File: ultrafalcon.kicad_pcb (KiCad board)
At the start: 2 copper layers, 66.3 x 66.3 mm, 1 part, among them SW1 RotaryEncoder

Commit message: jan17 updates
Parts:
- added C1: 0.01uF, ct-kicad:C0402, F.Cu at (147.5, 127.2)
- added C2: 0.01uF, ct-kicad:C0402, F.Cu at (152.5, 127.2)
- added C3: 1uF, ct-kicad:C0402, F.Cu at (158.6, 103.1)
- added H1: MountingHole, MountingHole:MountingHole_3.2mm_M3_Pad_Via, F.Cu at (143.5, 112.0)
- added H2: MountingHole, MountingHole:MountingHole_3.2mm_M3_Pad_Via, F.Cu at (143.5, 87.0)
- added J1: Conn_01x08_Socket, Connector_JST:JST_EH_B8B-EH-A_1x08_P2.50mm_Vertical, F.Cu at (160.0, 100.0)
- added R1: 330, ct-kicad:R0603, F.Cu at (158.2, 127.0)
- added R2: 10k, ct-kicad:R0603, F.Cu at (154.2, 127.0)
- added R3: 10k, ct-kicad:R0603, F.Cu at (145.8, 127.0)
- added R4: 10k, ct-kicad:R0603, F.Cu at (155.9, 127.0)
- added R5: 10k, ct-kicad:R0603, F.Cu at (144.1, 127.0)
- added U1: SK6812MINI-E_C5149201, ct-kicad:YS-SK6812MINI-E-casuanoob, F.Cu at (141.1, 66.9)
- added U10: SK6812MINI-E_C5149201, ct-kicad:YS-SK6812MINI-E-casuanoob, F.Cu at (116.7, 109.2)
- added U11: SK6812MINI-E_C5149201, ct-kicad:YS-SK6812MINI-E-casuanoob, F.Cu at (116.7, 91.3)
- added U12: SK6812MINI-E_C5149201, ct-kicad:YS-SK6812MINI-E-casuanoob, F.Cu at (125.6, 75.9)
- added U13: SK6812MINI-E_C5149201, ct-kicad:YS-SK6812MINI-E-casuanoob, F.Cu at (134.6, 108.5)
- added U14: SK6812MINI-E_C5149201, ct-kicad:YS-SK6812MINI-E-casuanoob, F.Cu at (134.9, 90.9)
- added U15: SK6812MINI-E_C5149201, ct-kicad:YS-SK6812MINI-E-casuanoob, F.Cu at (150.4, 82.4)
- added U16: SK6812MINI-E_C5149201, ct-kicad:YS-SK6812MINI-E-casuanoob, F.Cu at (165.4, 91.5)
- added U17: SK6812MINI-E_C5149201, ct-kicad:YS-SK6812MINI-E-casuanoob, F.Cu at (165.1, 109.1)
- added U18: SK6812MINI-E_C5149201, ct-kicad:YS-SK6812MINI-E-casuanoob, F.Cu at (149.6, 117.6)
- added U2: SK6812MINI-E_C5149201, ct-kicad:YS-SK6812MINI-E-casuanoob, F.Cu at (158.9, 66.9)
- added U3: SK6812MINI-E_C5149201, ct-kicad:YS-SK6812MINI-E-casuanoob, F.Cu at (174.4, 75.9)
- added U4: SK6812MINI-E_C5149201, ct-kicad:YS-SK6812MINI-E-casuanoob, F.Cu at (183.3, 91.3)
- added U5: SK6812MINI-E_C5149201, ct-kicad:YS-SK6812MINI-E-casuanoob, F.Cu at (183.3, 109.2)
- added U6: SK6812MINI-E_C5149201, ct-kicad:YS-SK6812MINI-E-casuanoob, F.Cu at (174.4, 124.7)
- added U7: SK6812MINI-E_C5149201, ct-kicad:YS-SK6812MINI-E-casuanoob, F.Cu at (158.9, 133.6)
- added U8: SK6812MINI-E_C5149201, ct-kicad:YS-SK6812MINI-E-casuanoob, F.Cu at (141.1, 133.6)
- added U9: SK6812MINI-E_C5149201, ct-kicad:YS-SK6812MINI-E-casuanoob, F.Cu at (125.6, 124.7)
- SW1: footprint fingerpunch:PERS56v3 -> ct-kicad:PER60
- moved SW1 2.20 mm to (150.0, 100.0)
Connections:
- SW1 pad A: unconnected-(SW1-PadA) -> Net-(C2-Pad1)
- SW1 pad B: unconnected-(SW1-PadB) -> Net-(C1-Pad1)
- SW1 pad C: unconnected-(SW1-PadC) -> GND
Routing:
- net Net-(U13-DIN): track 0.00 -> 50.5 mm, vias 0 -> 2
- net ENCODER_B: track 0.00 -> 43.7 mm, vias 0 -> 2
- net LED_DO: track 0.00 -> 35.0 mm
- net ENCODER_A: track 0.00 -> 33.7 mm, vias 0 -> 2
- net LED_DI: track 0.00 -> 29.9 mm
- net Net-(U17-DOUT): track 0.00 -> 17.3 mm, vias 0 -> 2
- net Net-(U14-DOUT): track 0.00 -> 16.1 mm
- net Net-(U1-DOUT): track 0.00 -> 14.3 mm
- net Net-(U15-DOUT): track 0.00 -> 14.1 mm
- net Net-(U16-DOUT): track 0.00 -> 13.8 mm
- net Net-(U13-DOUT): track 0.00 -> 13.6 mm
- net Net-(U7-DIN): track 0.00 -> 13.6 mm
- net Net-(U11-DOUT): track 0.00 -> 13.6 mm
- net Net-(U2-DOUT): track 0.00 -> 13.6 mm
- net Net-(U5-DOUT): track 0.00 -> 13.6 mm
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- added copper zone on B.Cu, net GND
- added copper zone on F.Cu, net GND
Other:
- board size 66.3 x 66.3 mm -> 77 x 77 mm

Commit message: v5
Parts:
- removed the U4 at (183.3, 91.3)
- added SW2: SW_Push, ct-kicad:SW_MX_cutout, F.Cu at (150.0, 100.0)
- added U18: SK6805-EC15, ct-kicad:LED-SMD_4P-L1.5-W1.5-BL, F.Cu at (183.6, 108.8)
- added U19: SK6805-EC15, ct-kicad:LED-SMD_4P-L1.5-W1.5-BL, F.Cu at (180.1, 117.2)
- added U20: SK6805-EC15, ct-kicad:LED-SMD_4P-L1.5-W1.5-BL, F.Cu at (174.7, 124.4)
- added U21: SK6805-EC15, ct-kicad:LED-SMD_4P-L1.5-W1.5-BL, F.Cu at (167.5, 130.0)
- added U22: SK6805-EC15, ct-kicad:LED-SMD_4P-L1.5-W1.5-BL, F.Cu at (159.1, 133.5)
- added U23: SK6805-EC15, ct-kicad:LED-SMD_4P-L1.5-W1.5-BL, F.Cu at (150.2, 134.7)
- added U24: SK6805-EC15, ct-kicad:LED-SMD_4P-L1.5-W1.5-BL, F.Cu at (141.2, 133.6)
- added U25: SK6805-EC15, ct-kicad:LED-SMD_4P-L1.5-W1.5-BL, F.Cu at (132.8, 130.1)
- added U27: SK6805-EC15, ct-kicad:LED-SMD_4P-L1.5-W1.5-BL, F.Cu at (120.0, 117.5)
- added U28: SK6805-EC15, ct-kicad:LED-SMD_4P-L1.5-W1.5-BL, F.Cu at (116.5, 109.1)
- added U29: SK6805-EC15, ct-kicad:LED-SMD_4P-L1.5-W1.5-BL, F.Cu at (115.3, 100.2)
- added U30: SK6805-EC15, ct-kicad:LED-SMD_4P-L1.5-W1.5-BL, F.Cu at (116.4, 91.2)
- added U9: SK6805-EC15, ct-kicad:LED-SMD_4P-L1.5-W1.5-BL, F.Cu at (132.5, 70.0)
- C1, C2: value 0.01uF -> CL05B104KO5NNNC
- C3: value 1uF -> CL05B104KO5NNNC
- J1: moved to B.Cu
- R1: value 330 -> 0603WAF3300T5E
- R2, R3, R4, R5: value 10k -> 0603WAF3300T5E
- U1, U10, U11, U12, U13, U14, U15, U16, U17, U2, U3, U5, U6, U7, U8: value SK6812MINI-E_C5149201 -> SK6805-EC15; footprint ct-kicad:YS-SK6812MINI-E-casuanoob -> ct-kicad:LED-SMD_4P-L1.5-W1.5-BL
- U26: renamed from U9; value SK6812MINI-E_C5149201 -> SK6805-EC15; footprint ct-kicad:YS-SK6812MINI-E-casuanoob -> ct-kicad:LED-SMD_4P-L1.5-W1.5-BL
- U4: renamed from U18; value SK6812MINI-E_C5149201 -> SK6805-EC15; footprint ct-kicad:YS-SK6812MINI-E-casuanoob -> ct-kicad:LED-SMD_4P-L1.5-W1.5-BL
- moved U7 64.1 mm to (119.9, 82.8), turned to 180 degrees
- moved U8 60.1 mm to (125.3, 75.6), turned to 180 degrees
- moved U6 54.3 mm to (132.6, 89.9), turned to 180 degrees
- moved U5 50.7 mm to (132.6, 110.0), turned to 180 degrees
- moved U13 50.5 mm to (167.2, 69.9), turned to 180 degrees
- moved U10 49.0 mm to (140.9, 66.5), turned to 180 degrees
- moved U14 42.4 mm to (174.4, 75.3), turned to 180 degrees
- moved U11 42.2 mm to (149.8, 65.3), turned to 180 degrees
- moved C1 38.8 mm to (169.7, 95.4)
- moved R3 37.1 mm to (169.8, 98.6), turned to -90 degrees
- moved R5 37.1 mm to (168.0, 98.6), turned to -90 degrees
- moved U3 34.9 mm to (167.4, 110.1), turned to 180 degrees
- moved U12 34.5 mm to (158.8, 66.4), turned to 180 degrees
- moved H2 29.8 mm to (158.0, 113.0)
- moved R2 29.6 mm to (169.8, 101.8)
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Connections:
- R1 pad 2: Net-(U7-DIN) -> Net-(U1-DIN)
- U1 pad 1: VCC -> GND
- U1 pad 2: Net-(U1-DOUT) -> Net-(U1-DIN)
- U1 pad 3: GND -> Net-(U1-DOUT)
- U1 pad 4: Net-(U1-DIN) -> VCC
- U10 pad 1: VCC -> GND
- U10 pad 2: Net-(U10-DOUT) -> Net-(U10-VDD)
- U10 pad 3: GND -> Net-(U10-DOUT)
- U10 pad 4: Net-(U10-DIN) -> VCC
- U11 pad 1: VCC -> GND
- U11 pad 2: Net-(U11-DOUT) -> Net-(U10-DOUT)
- U11 pad 3: GND -> Net-(U11-DOUT)
- U11 pad 4: Net-(U10-DOUT) -> VCC
- U12 pad 1: VCC -> GND
- U12 pad 2: Net-(U1-DIN) -> Net-(U11-DOUT)
- U12 pad 3: GND -> Net-(U12-DOUT)
- U12 pad 4: Net-(U11-DOUT) -> VCC
- U13 pad 1: VCC -> GND
- U13 pad 2: Net-(U13-DOUT) -> Net-(U12-DOUT)
- U13 pad 3: GND -> Net-(U13-DOUT)
- U13 pad 4: Net-(U13-DIN) -> VCC
- U14 pad 1: VCC -> GND
- U14 pad 2: Net-(U14-DOUT) -> Net-(U13-DOUT)
- U14 pad 3: GND -> Net-(U14-DOUT)
- U14 pad 4: Net-(U13-DOUT) -> VCC
- U15 pad 1: VCC -> GND
- U15 pad 2: Net-(U15-DOUT) -> Net-(U14-DOUT)
- U15 pad 3: GND -> Net-(U15-DOUT)
- U15 pad 4: Net-(U14-DOUT) -> VCC
- U16 pad 1: VCC -> GND
- U16 pad 2: Net-(U16-DOUT) -> Net-(U15-DOUT)
- U16 pad 3: GND -> Net-(U16-DOUT)
- U16 pad 4: Net-(U15-DOUT) -> VCC
- U17 pad 1: VCC -> GND
- U17 pad 2: Net-(U17-DOUT) -> Net-(U16-DOUT)
- U17 pad 3: GND -> Net-(U17-DOUT)
- U17 pad 4: Net-(U16-DOUT) -> VCC
- U2 pad 1: VCC -> GND
- U2 pad 2: Net-(U2-DOUT) -> Net-(U1-DOUT)
- U2 pad 3: GND -> Net-(U2-DOUT)
- U2 pad 4: Net-(U1-DOUT) -> VCC
- U26 pad 1: VCC -> GND
- U26 pad 2: Net-(U10-DIN) -> Net-(U25-DOUT)
- U26 pad 3: GND -> Net-(U26-DOUT)
- U26 pad 4: Net-(U8-DOUT) -> VCC
- U3 pad 1: VCC -> GND
- U3 pad 2: Net-(U3-DOUT) -> Net-(U2-DOUT)
- U3 pad 3: GND -> Net-(U3-DOUT)
- U3 pad 4: Net-(U2-DOUT) -> VCC
- U4 pad 1: VCC -> GND
- U4 pad 2: LED_DO -> Net-(U3-DOUT)
- U4 pad 3: GND -> Net-(U4-DOUT)
- U4 pad 4: Net-(U17-DOUT) -> VCC
- U5 pad 1: VCC -> GND
- U5 pad 2: Net-(U5-DOUT) -> Net-(U4-DOUT)
- U5 pad 3: GND -> Net-(U5-DOUT)
- U5 pad 4: Net-(U4-DOUT) -> VCC
- U6 pad 1: VCC -> GND
- U6 pad 2: Net-(U13-DIN) -> Net-(U5-DOUT)
- U6 pad 3: GND -> LED_TO_OUTER_CHAIN
- U6 pad 4: Net-(U5-DOUT) -> VCC
- U7 pad 1: VCC -> GND
- U7 pad 2: Net-(U7-DOUT) -> LED_TO_OUTER_CHAIN
- U7 pad 3: GND -> Net-(U7-DOUT)
- U7 pad 4: Net-(U7-DIN) -> VCC
- U8 pad 1: VCC -> GND
- U8 pad 2: Net-(U8-DOUT) -> Net-(U7-DOUT)
- U8 pad 3: GND -> Net-(U8-DOUT)
- U8 pad 4: Net-(U7-DOUT) -> VCC
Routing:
- net Net-(U13-DIN): track 50.5 -> 0.00 mm, vias 2 -> 0
- net ENCODER_B: track 43.7 -> 0.00 mm, vias 2 -> 0
- net LED_DO: track 35.0 -> 0.00 mm
- net ENCODER_A: track 33.7 -> 0.00 mm, vias 2 -> 0
- net LED_DI: track 29.9 -> 0.00 mm
- net Net-(U17-DOUT): track 17.3 -> 0.00 mm, vias 2 -> 0
- net Net-(U14-DOUT): track 16.1 -> 0.00 mm
- net Net-(U1-DOUT): track 14.3 -> 0.00 mm
- net Net-(U15-DOUT): track 14.1 -> 0.00 mm
- net Net-(U16-DOUT): track 13.8 -> 0.00 mm
- net Net-(U13-DOUT): track 13.6 -> 0.00 mm
- net Net-(U7-DIN): track 13.6 -> 0.00 mm
- net Net-(U11-DOUT): track 13.6 -> 0.00 mm
- net Net-(U2-DOUT): track 13.6 -> 0.00 mm
- net Net-(U5-DOUT): track 13.6 -> 0.00 mm
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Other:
- outline, holes or cut-outs redrawn

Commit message: ready for first review
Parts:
- moved R1 19.7 mm to (153.2, 80.2), turned to 180 degrees
- moved C3 1.05 mm to (167.0, 105.5)
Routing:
- net VCC: track 0.00 -> 102.8 mm, vias 0 -> 35
- net LED_DO: track 0.00 -> 51.8 mm, vias 0 -> 1
- net Net-(C2-Pad1): track 0.00 -> 48.8 mm, vias 0 -> 2
- net Net-(C1-Pad1): track 0.00 -> 46.5 mm, vias 0 -> 2
- net Net-(U1-DOUT): track 0.00 -> 33.7 mm, vias 0 -> 2
- net Net-(U3-DOUT): track 0.00 -> 33.6 mm, vias 0 -> 2
- net Net-(U2-DOUT): track 0.00 -> 25.6 mm, vias 0 -> 2
- net LED_DI: track 0.00 -> 22.7 mm, vias 0 -> 2
- net Net-(U5-DOUT): track 0.00 -> 21.0 mm, vias 0 -> 2
- net Net-(U4-DOUT): track 0.00 -> 20.2 mm, vias 0 -> 2
- net Net-(U14-DOUT): track 0.00 -> 17.7 mm, vias 0 -> 2
- net Net-(U15-DOUT): track 0.00 -> 17.5 mm, vias 0 -> 2
- net Net-(U13-DOUT): track 0.00 -> 17.2 mm, vias 0 -> 2
- net Net-(U16-DOUT): track 0.00 -> 15.7 mm, vias 0 -> 2
- net Net-(U12-DOUT): track 0.00 -> 15.4 mm, vias 0 -> 2
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- added copper zone on B.Cu, net VCC
- removed copper zone on B.Cu, net GND
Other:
- board size 77 x 77 mm -> 78 x 78 mm

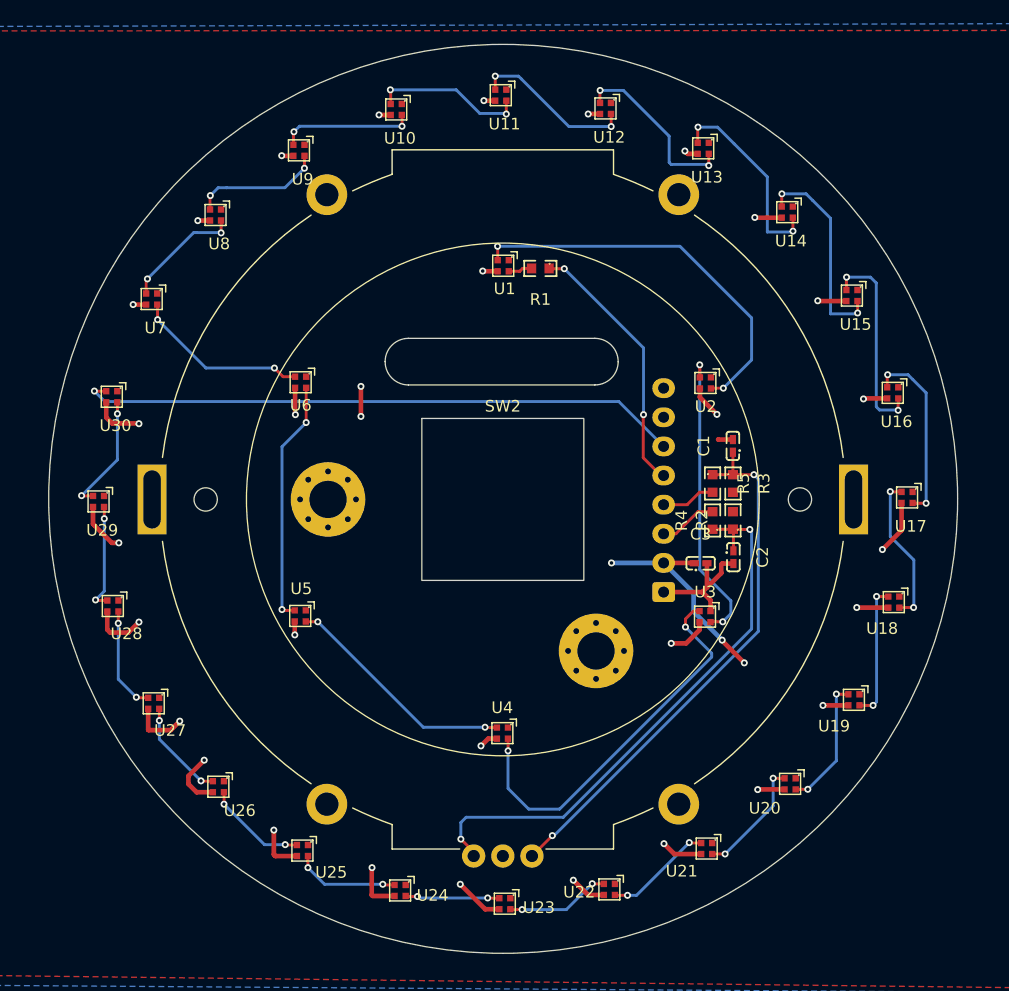
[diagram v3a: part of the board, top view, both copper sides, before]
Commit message: replacing the led footprint and symbol, doing the tracing
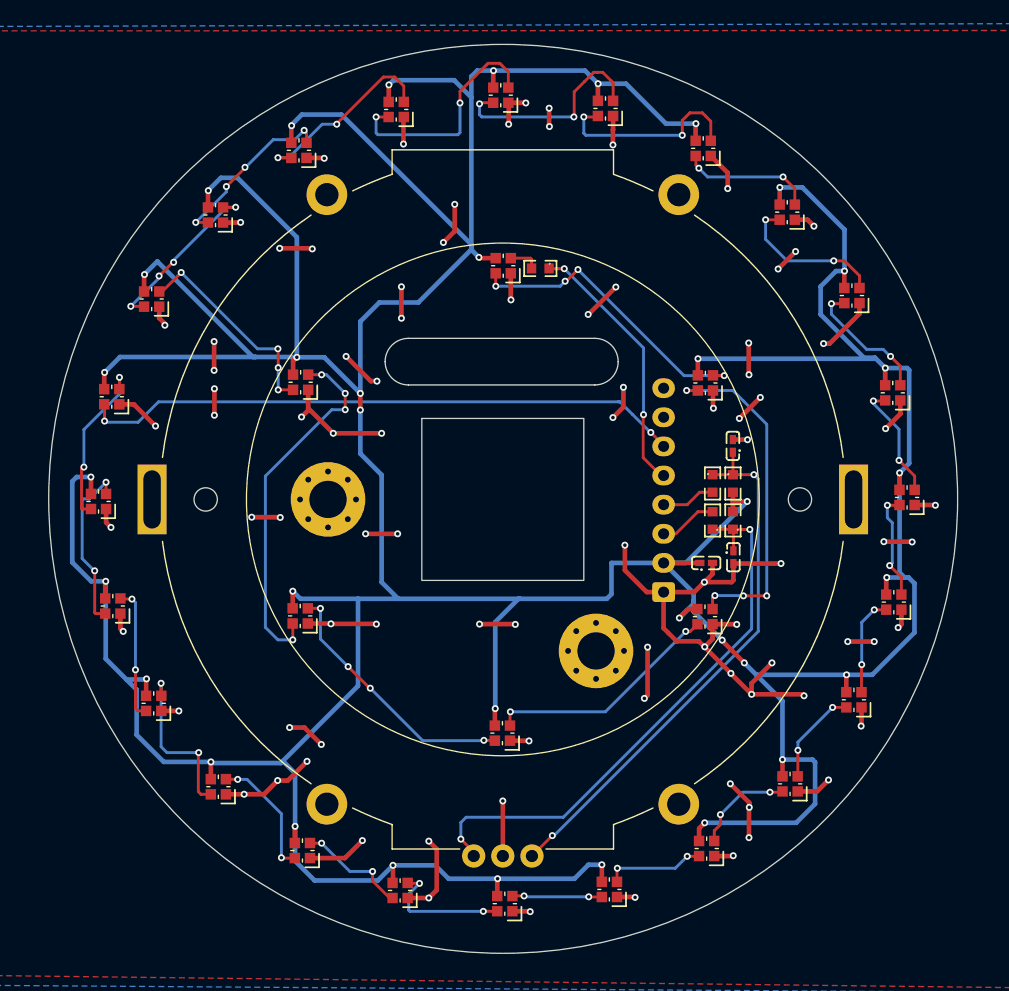
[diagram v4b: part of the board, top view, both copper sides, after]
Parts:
- U1, U10, U11, U12, U13, U14, U15, U16, U17, U18, U19, U2, U20, U21, U22, U23, U24, U25, U26, U27, U28, U29, U3, U30, U4, U5, U6, U7, U8, U9: footprint ct-kicad:LED-SMD_4P-L1.5-W1.5-BL -> ct-kicad:LED_dilemma_SK6805-EC15_1.5x1.5mm_P0.6mm_handsolder
- moved C3 0.48 mm to (167.4, 105.5)
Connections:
- U1 pad 1: GND -> Net-(U1-DIN)
- U1 pad 2: Net-(U1-DIN) -> VCC
- U1 pad 4: VCC -> GND
- U10 pad 1: GND -> Net-(U10-DIN)
- U10 pad 2: Net-(U10-VDD) -> VCC
- U10 pad 4: VCC -> GND
- U11 pad 1: GND -> Net-(U10-DOUT)
- U11 pad 2: Net-(U10-DOUT) -> VCC
- U11 pad 4: VCC -> GND
- U12 pad 1: GND -> Net-(U11-DOUT)
- U12 pad 2: Net-(U11-DOUT) -> VCC
- U12 pad 4: VCC -> GND
- U13 pad 1: GND -> Net-(U12-DOUT)
- U13 pad 2: Net-(U12-DOUT) -> VCC
- U13 pad 4: VCC -> GND
- U14 pad 1: GND -> Net-(U13-DOUT)
- U14 pad 2: Net-(U13-DOUT) -> VCC
- U14 pad 4: VCC -> GND
- U15 pad 1: GND -> Net-(U14-DOUT)
- U15 pad 2: Net-(U14-DOUT) -> VCC
- U15 pad 4: VCC -> GND
- U16 pad 1: GND -> Net-(U15-DOUT)
- U16 pad 2: Net-(U15-DOUT) -> VCC
- U16 pad 4: VCC -> GND
- U17 pad 1: GND -> Net-(U16-DOUT)
- U17 pad 2: Net-(U16-DOUT) -> VCC
- U17 pad 4: VCC -> GND
- U18 pad 1: GND -> Net-(U17-DOUT)
- U18 pad 2: Net-(U17-DOUT) -> VCC
- U18 pad 4: VCC -> GND
- U19 pad 1: GND -> Net-(U18-DOUT)
- U19 pad 2: Net-(U18-DOUT) -> VCC
- U19 pad 4: VCC -> GND
- U2 pad 1: GND -> Net-(U1-DOUT)
- U2 pad 2: Net-(U1-DOUT) -> VCC
- U2 pad 4: VCC -> GND
- U20 pad 1: GND -> Net-(U19-DOUT)
- U20 pad 2: Net-(U19-DOUT) -> VCC
- U20 pad 4: VCC -> GND
- U21 pad 1: GND -> Net-(U20-DOUT)
- U21 pad 2: Net-(U20-DOUT) -> VCC
- U21 pad 4: VCC -> GND
- U22 pad 1: GND -> Net-(U21-DOUT)
- U22 pad 2: Net-(U21-DOUT) -> VCC
- U22 pad 4: VCC -> GND
- U23 pad 1: GND -> Net-(U22-DOUT)
- U23 pad 2: Net-(U22-DOUT) -> VCC
- U23 pad 4: VCC -> GND
- U24 pad 1: GND -> Net-(U23-DOUT)
- U24 pad 2: Net-(U23-DOUT) -> VCC
- U24 pad 4: VCC -> GND
- U25 pad 1: GND -> Net-(U24-DOUT)
- U25 pad 2: Net-(U24-DOUT) -> VCC
- U25 pad 4: VCC -> GND
- U26 pad 1: GND -> Net-(U25-DOUT)
- U26 pad 2: Net-(U25-DOUT) -> VCC
- U26 pad 4: VCC -> GND
- U27 pad 1: GND -> Net-(U26-DOUT)
- U27 pad 2: Net-(U26-DOUT) -> VCC
- U27 pad 4: VCC -> GND
- U28 pad 1: GND -> Net-(U27-DOUT)
- U28 pad 2: Net-(U27-DOUT) -> VCC
- U28 pad 4: VCC -> GND
- U29 pad 1: GND -> Net-(U28-DOUT)
- U29 pad 2: Net-(U28-DOUT) -> VCC
- U29 pad 4: VCC -> GND
- U3 pad 1: GND -> Net-(U2-DOUT)
- U3 pad 2: Net-(U2-DOUT) -> VCC
- U3 pad 4: VCC -> GND
- U30 pad 1: GND -> Net-(U29-DOUT)
- U30 pad 2: Net-(U29-DOUT) -> VCC
- U30 pad 4: VCC -> GND
- U4 pad 1: GND -> Net-(U3-DOUT)
- U4 pad 2: Net-(U3-DOUT) -> VCC
- U4 pad 4: VCC -> GND
- U5 pad 1: GND -> Net-(U4-DOUT)
- U5 pad 2: Net-(U4-DOUT) -> VCC
- U5 pad 4: VCC -> GND
- U6 pad 1: GND -> Net-(U5-DOUT)
- U6 pad 2: Net-(U5-DOUT) -> VCC
- U6 pad 4: VCC -> GND
- U7 pad 1: GND -> LED_TO_OUTER_CHAIN
- U7 pad 2: LED_TO_OUTER_CHAIN -> VCC
- U7 pad 4: VCC -> GND
- U8 pad 1: GND -> Net-(U7-DOUT)
- U8 pad 2: Net-(U7-DOUT) -> VCC
- U8 pad 4: VCC -> GND
- U9 pad 1: GND -> Net-(U8-DOUT)
- U9 pad 2: Net-(U8-DOUT) -> VCC
- U9 pad 3: Net-(U10-VDD) -> Net-(U10-DIN)
- U9 pad 4: VCC -> GND
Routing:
- net VCC: track 102.8 -> 482.8 mm
- net GND: track 12.7 -> 200.0 mm, vias 0 -> 88
- net Net-(U10-DIN): track 0.00 -> 16.5 mm, vias 0 -> 2
- net Net-(U3-DOUT): track 33.6 -> 20.4 mm
- net Net-(U10-VDD): track 11.6 -> 0.00 mm, vias 2 -> 0
- net Net-(U5-DOUT): track 21.0 -> 31.6 mm, vias 2 -> 4
- net Net-(U1-DOUT): track 33.7 -> 26.0 mm, vias 2 -> 4
- net Net-(U10-DOUT): track 13.2 -> 20.1 mm
- net Net-(U15-DOUT): track 17.5 -> 11.4 mm
- net Net-(U26-DOUT): track 8.69 -> 14.5 mm
- net Net-(U13-DOUT): track 17.2 -> 11.5 mm
- net Net-(U16-DOUT): track 15.7 -> 10.1 mm
- net Net-(U28-DOUT): track 9.32 -> 14.8 mm
- net Net-(U7-DOUT): track 10.3 -> 15.0 mm, vias 2 -> 4
- net Net-(U11-DOUT): track 14.0 -> 18.4 mm
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- added copper zone on B.Cu, net GND
- removed copper zone on B.Cu, net VCC

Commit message: moving text around, adding rear labels, updating footprints
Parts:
- added LOGO1: **REF, ct-kicad:awesome-logo, B.Cu at (120.6, 90.2)
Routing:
- net GND: track 200.0 -> 215.1 mm, vias 88 -> 92
- net Net-(U10-DIN): track 16.5 -> 16.6 mm, vias 2 -> 4
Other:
- board text added: "+5V"
- board text added: "ENC_A"
- board text added: "ENC_B"
- board text added: "GND"
- board text added: "LED_DI"
- board text added: "LED_DO"
- board text added: "SW_A"
- board text added: "SW_B"
- board text added: "UltraFalcon"
- board text added: "v1.0"
